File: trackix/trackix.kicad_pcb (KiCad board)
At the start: 2 copper layers, 87.6 x 114.3 mm, 42 parts, among them IC1 SIM808, J1 GSM, J2 GPS, J3 SIM5060-6-0-26-01-X_REVC, J4 AVR-ISP-6, Q1 2N3904, Q2 2N3904, U1 ATmega328P-AU

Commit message: layout changes 1
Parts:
- removed 8MHz1: Crystal, Crystal:Crystal_SMD_HC49-SD_HandSoldering
- removed D1: netstat LED, LED_SMD:LED_0805_2012Metric_Pad1.15x1.40mm_HandSolder
- removed D2: led 13, LED_SMD:LED_0805_2012Metric_Pad1.15x1.40mm_HandSolder
- removed D3: ISP led, LED_SMD:LED_0805_2012Metric_Pad1.15x1.40mm_HandSolder
- removed reset1: reset, Button_Switch_SMD:SW_SPST_TL3342
- added 13_blk: led 13, LED_SMD:LED_0805_2012Metric_Pad1.15x1.40mm_HandSolder, F.Cu at (102.2, 41.3)
- added 8MHz: Crystal, Crystals:Crystal_HC49-4H_Vertical, F.Cu at (129.2, 66.9)
- added ISP_pwr: ISP led, LED_SMD:LED_0805_2012Metric_Pad1.15x1.40mm_HandSolder, F.Cu at (102.2, 38.7)
- added RESET: reset, Buttons_Switches_SMD:SW_SPST_B3U-1000P, F.Cu at (128.3, 41.9)
- added netstat: netstat LED, LED_SMD:LED_0805_2012Metric_Pad1.15x1.40mm_HandSolder, F.Cu at (69.8, 38.7)
- J3: value SIM5060-6-0-26-01-X_REVC -> SIM CARD; footprint SIM5060-6-0-26-01-X_REVC:GCT_SIM5060-6-0-26-01-X_REVC -> SIM7100-6-1-15-00-X_REVA:GCT_SIM7100-6-1-15-00-X_REVA
- LS1: value CBT-09427-SMT -> buzzer
- moved BT1 194.6 mm to (52.7, 69.8), turned to 270 degrees
- moved C9 193.9 mm to (52.2, 54.3)
- moved C8 190.1 mm to (52.2, 56.9)
- moved C14 189.6 mm to (50.8, 67.3), turned to 180 degrees
- moved R4 186.9 mm to (65.4, 40.6), turned to 22 degrees
- moved JP1 185.6 mm to (61.0, 65.4), turned to 22 degrees
- moved R7 165.4 mm to (97.8, 41.3), turned to 180 degrees
- moved LS1 165.2 mm to (115.6, 49.5), turned to 90 degrees
- moved Q1 163.6 mm to (116.2, 40.0)
- moved R5 163.1 mm to (111.8, 40.0), turned to 90 degrees
- moved C6 160.6 mm to (52.8, 61.9)
- moved C13 160.0 mm to (51.4, 64.8), turned to 180 degrees
- moved C7 157.4 mm to (52.8, 59.4)
- moved C12 145.3 mm to (112.4, 67.5), turned to 270 degrees
- moved R8 136.1 mm to (97.8, 38.7)
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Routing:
- net Net-(J4-Pad2): track 0.00 -> 90.9 mm, vias 0 -> 2
- net Net-(D4-Pad1): track 0.00 -> 84.7 mm, vias 0 -> 1
- net Net-(C2-Pad1): track 0.00 -> 44.3 mm
- net Net-(J4-Pad3): track 0.00 -> 43.2 mm, vias 0 -> 1
- net Net-(R9-Pad1): track 0.00 -> 42.5 mm, vias 0 -> 4
- net Net-(J4-Pad5): track 0.00 -> 38.5 mm, vias 0 -> 3
- net Net-(R5-Pad1): track 0.00 -> 32.8 mm, vias 0 -> 4
- net Net-(J3-PadC7): track 0.00 -> 19.2 mm
- net Net-(J3-PadC2): track 0.00 -> 17.3 mm
- net Net-(C1-Pad1): track 0.00 -> 15.9 mm
- net Net-(C3-Pad1): track 0.00 -> 15.6 mm
- net Net-(J3-PadC3): track 0.00 -> 13.9 mm
- net +BATT: track 0.00 -> 13.3 mm
- net Net-(D1-Pad2): track 0.00 -> 12.9 mm
- net Net-(C4-Pad1): track 0.00 -> 12.9 mm
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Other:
- board size 87.6 x 114.3 mm -> 85.1 x 43.2 mm

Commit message: layout changes 2
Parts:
- removed 13_blk: led 13, LED_SMD:LED_0805_2012Metric_Pad1.15x1.40mm_HandSolder
- removed ISP_pwr: ISP led, LED_SMD:LED_0805_2012Metric_Pad1.15x1.40mm_HandSolder
- removed the netstat at (69.8, 38.7)
- added ISPpwr: ISP led, LEDs:LED_0805_HandSoldering, F.Cu at (102.2, 38.7)
- added R10: 470, Resistors_SMD:R_0805_HandSoldering, F.Cu at (52.7, 44.5)
- added R11: 470, Resistors_SMD:R_0805_HandSoldering, F.Cu at (126.4, 45.7)
- added R12: 470, Resistors_SMD:R_0805_HandSoldering, F.Cu at (97.8, 48.9)
- added blk: led 13, LEDs:LED_0805_HandSoldering, F.Cu at (102.2, 41.3)
- added netstat: netstat LED, LEDs:LED_0805_HandSoldering, F.Cu at (70.5, 38.7)
- J3: value SIM CARD -> SIM SLOT
- LS1: value buzzer -> BUZZER
- moved R4 0.63 mm to (65.4, 41.3)
- moved RESET 0.63 mm to (128.9, 41.9)
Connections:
- D4 pad 2: +BATT -> Net-(D4-Pad2)
- D5 pad 2: +BATT -> Net-(D5-Pad2)
- D6 pad 2: +BATT -> Net-(D6-Pad2)
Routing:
- net GND: track 0.00 -> 142.3 mm, vias 0 -> 43
- net +BATT: track 13.3 -> 89.8 mm, vias 0 -> 2
- net simTX: track 0.00 -> 59.2 mm, vias 0 -> 2
- net simRX: track 0.00 -> 58.7 mm, vias 0 -> 3
- net Net-(D4-Pad2): track 0.00 -> 9.41 mm
- net Net-(D6-Pad2): track 0.00 -> 5.94 mm
- net Net-(J4-Pad5): track 38.5 -> 43.6 mm, vias 3 -> 2
- net Net-(D5-Pad2): track 0.00 -> 3.21 mm
- net Net-(D1-Pad2): track 12.9 -> 12.0 mm
- net Net-(D1-Pad1): track 3.10 -> 3.67 mm
- net Net-(R9-Pad1): track 42.5 -> 42.6 mm, vias 4 -> 3
- added copper zone on B.Cu, net GND

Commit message: prototype 0.1 state
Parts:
- added G***: LOGO, Logo:LOGO, B.Cu at (74.9, 55.9)
- added U2: SIM-ST-MFF2, SIM-ST-MFF2:PSON127P500X600X82-9N, B.Cu at (102.2, 61.6)
- moved R12 2.54 mm to (97.8, 51.4), turned to 90 degrees
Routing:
- net +BATT: track 89.8 -> 156.5 mm
- net GND: track 142.3 -> 169.2 mm, vias 43 -> 44
- net Net-(J3-PadC3): track 13.9 -> 27.3 mm, vias 0 -> 1
- net Net-(J3-PadC2): track 17.3 -> 28.6 mm, vias 0 -> 1
- net Net-(C2-Pad1): track 44.3 -> 55.6 mm, vias 0 -> 1
- net Net-(J3-PadC7): track 19.2 -> 27.9 mm, vias 0 -> 1
- net (no net): track 7.47 -> 0.37 mm
- net Net-(D6-Pad2): track 5.94 -> 7.84 mm
- net Net-(J3-PadC6): track 0.00 -> 1.73 mm, vias 0 -> 1
- added copper zone on F.Cu, net +BATT
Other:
- outline, holes or cut-outs redrawn
- board text added: "trackix v.0.1 2019-02-18"

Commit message: all things so far
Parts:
- removed 8MHz: Crystal, Crystals:Crystal_HC49-4H_Vertical
- removed BT1: Li-Ion 3,7v, Connector_PinHeader_2.54mm:PinHeader_1x02_P2.54mm_Horizontal
- removed IC1: SIM808, QFN100P2400X2400X260-68N
- removed ISPpwr: ISP led, LEDs:LED_0805_HandSoldering
- removed LS1: BUZZER, CUI_CBT-09427-SMT
- removed Q2: 2N3904, Package_TO_SOT_SMD:SOT-23_Handsoldering
- removed R3: 22, Resistor_SMD:R_0805_2012Metric_Pad1.15x1.40mm_HandSolder
- removed R4: 470, Resistor_SMD:R_0805_2012Metric_Pad1.15x1.40mm_HandSolder
- removed RESET: reset, Buttons_Switches_SMD:SW_SPST_B3U-1000P
- removed blk: led 13, LEDs:LED_0805_HandSoldering
- removed netstat: netstat LED, LEDs:LED_0805_HandSoldering
- added 8MHz1: Crystal, Crystals:Crystal_HC49-U_Vertical, F.Cu at (106.2, 63.0)
- added BZ1: Buzzer, Buzzers_Beepers:Buzzer_Murata_PKMCS0909E4000-R1, F.Cu at (140.0, 65.8)
- added C15: 10uF, Capacitors_SMD:C_1206, F.Cu at (77.5, 60.5)
- added C16: 100nF, Capacitors_SMD:C_0603, F.Cu at (95.0, 65.5)
- added C17: C_100nF, Capacitors_SMD:C_0603, F.Cu at (114.5, 41.5)
- added D1: GPS_LED, LEDs:LED_0805, F.Cu at (116.8, 44.8)
- added D10: D_B5818WS SK, Diodes_SMD:D_SOD-323, F.Cu at (64.2, 65.8)
- added D11: D_B5818WS SK, Diodes_SMD:D_SOD-323, F.Cu at (67.8, 65.3)
- added D2: led 13, LEDs:LED_0805, F.Cu at (115.8, 68.5)
- added D3: D_B5818WS SK, Diodes_SMD:D_SOD-323, F.Cu at (64.5, 68.2)
- added D7: LED_chrg, LEDs:LED_0805, F.Cu at (64.2, 63.7)
- added D8: LED_stdby, LEDs:LED_0805, F.Cu at (64.2, 61.7)
- added D9: D_B5818WS SK, Diodes_SMD:D_SOD-323, F.Cu at (68.2, 68.2)
- added H1: DYNAMO_A, Mounting_Holes:MountingHole_2.2mm_M2_ISO14580_Pad, F.Cu at (71.5, 76.5)
- added H2: DYNAMO_B, Mounting_Holes:MountingHole_2.2mm_M2_ISO14580_Pad, F.Cu at (77.2, 76.5)
- added IC2: TP4056, Housings_SOIC:HTSOP-8-1EP_3.9x4.9mm_Pitch1.27mm_ThermalVias_LargeCopper, F.Cu at (78.0, 64.8)
- added JP3: MOSI, Jumper:SolderJumper-2_P1.3mm_Open_RoundedPad1.0x1.5mm, F.Cu at (95.0, 47.5)
- added JP4: MISO, Jumper:SolderJumper-2_P1.3mm_Open_RoundedPad1.0x1.5mm, F.Cu at (95.0, 49.8)
- added L1: L27nH, Inductors_SMD:L_0402, F.Cu at (138.5, 52.0)
- added L2: L2.2uH, Inductors_SMD:L_1210, F.Cu at (89.2, 68.2)
- added Q3: FS8205A, Housings_SSOP:TSSOP-8_4.4x3mm_Pitch0.65mm, F.Cu at (81.0, 55.8)
- added Q5: 2N3904, TO_SOT_Packages_SMD:SOT-23, F.Cu at (102.3, 50.0)
- added R13: 470, Resistors_SMD:R_0603, F.Cu at (68.5, 61.5)
- added R14: 470, Resistors_SMD:R_0603, F.Cu at (68.2, 59.8)
- added R15: 4k for Ibat 300mA, Resistors_SMD:R_0603, F.Cu at (83.2, 66.2)
- added R16: R100, Resistors_SMD:R_0603, F.Cu at (122.5, 60.0)
- added R17: R22, Resistors_SMD:R_0603, F.Cu at (137.5, 50.0)
- added R18: R100, Resistors_SMD:R_0603, F.Cu at (120.2, 45.8)
- added R19: R5k, Resistors_SMD:R_0603, F.Cu at (100.0, 61.2)
- added R20: R10k, Resistors_SMD:R_0603, F.Cu at (100.8, 64.2)
- added R21: 4.7k, Resistors_SMD:R_0603, F.Cu at (110.9, 36.9)
- added TP1: DYNAMO_A, Connectors_TestPoints:Test_Point_Pad_1.0x1.0mm, B.Cu at (71.5, 72.2)
- added TP2: DYNAMO_B, Connectors_TestPoints:Test_Point_Pad_1.0x1.0mm, B.Cu at (77.2, 72.2)
- added TP3: GND, Connectors_TestPoints:Test_Point_Pad_1.0x1.0mm, B.Cu at (87.3, 68.4)
- added TP4: VCC_IN_DC, Connectors_TestPoints:Test_Point_Pad_1.0x1.0mm, B.Cu at (102.0, 67.5)
- added TP5: AUX_ON, Connectors_TestPoints:Test_Point_Pad_1.0x1.0mm, B.Cu at (92.0, 60.0)
- added TP6: GPS_TX, Connectors_TestPoints:Test_Point_Pad_1.0x1.0mm, B.Cu at (125.0, 60.5)
- added TP7: TX, Connectors_TestPoints:Test_Point_Pad_1.0x1.0mm, B.Cu at (109.5, 52.0)
- added TP8: RX, Connectors_TestPoints:Test_Point_Pad_1.0x1.0mm, B.Cu at (104.5, 52.0)
- added TP9: TestPoint3.3V, Connectors_TestPoints:Test_Point_Pad_1.0x1.0mm, B.Cu at (92.3, 68.4)
- added U3: DW-01, TO_SOT_Packages_SMD:TSOT-23-6, F.Cu at (73.8, 57.2)
- added U4: TPS62291DRVR, user_added_kicad_libs:SON65P200X200X80-7N, F.Cu at (89.5, 64.8)
- added U5: RFM95W-868S2, RF_Modules:Hopref_RFM9XW_SMD, F.Cu at (82.5, 44.0)
- added U6: ADXL345BCCZ, Housings_LGA:Bosch_LGA-14_3x2.5mm_Pitch0.5mm, F.Cu at (114.5, 38.0)
- added reset1: reset, Buttons_Switches_SMD:SW_SPST_B3U-1000P, F.Cu at (144.5, 38.5)
- C1: value 22pF -> 100nF; footprint Capacitor_SMD:C_0805_2012Metric_Pad1.15x1.40mm_HandSolder -> Capacitors_SMD:C_0805
- C10, C11: footprint Capacitor_SMD:C_0805_2012Metric_Pad1.15x1.40mm_HandSolder -> Capacitors_SMD:C_0402
- C12: value 0,1uF -> 10uF; footprint Capacitor_SMD:C_0805_2012Metric_Pad1.15x1.40mm_HandSolder -> Capacitors_SMD:C_1206
- C13: footprint Capacitor_Tantalum_SMD:CP_EIA-3216-10_Kemet-I_Pad1.58x1.35mm_HandSolder -> Capacitors_SMD:C_0603
- C14: value 0,1uF -> 0.1uF; footprint Capacitor_SMD:C_0805_2012Metric_Pad1.15x1.40mm_HandSolder -> Capacitors_SMD:C_0603
- C2: value 1uF -> 10uF; footprint Capacitor_Tantalum_SMD:CP_EIA-3216-10_Kemet-I_Pad1.58x1.35mm_HandSolder -> Capacitors_SMD:C_1206
- C3: value 22pF -> C_100nF; footprint Capacitor_SMD:C_0805_2012Metric_Pad1.15x1.40mm_HandSolder -> Capacitors_SMD:C_0603
- C4: value 22pF -> C_4.7uF; footprint Capacitor_SMD:C_0805_2012Metric_Pad1.15x1.40mm_HandSolder -> Capacitors_SMD:C_1206
- C5: value 1uF -> C_100nF; footprint Capacitor_Tantalum_SMD:CP_EIA-3216-10_Kemet-I_Pad1.58x1.35mm_HandSolder -> Capacitors_SMD:C_0603
- C6: value 100uF -> C_4.7uF; footprint Capacitor_Tantalum_SMD:CP_EIA-3216-10_Kemet-I_Pad1.58x1.35mm_HandSolder -> Capacitors_SMD:C_1206
- C7: value 10uF -> C_100nF; footprint Capacitor_Tantalum_SMD:CP_EIA-3216-10_Kemet-I_Pad1.58x1.35mm_HandSolder -> Capacitors_SMD:C_0603
- C8: value 33pF -> 100nF; footprint Capacitor_SMD:C_0805_2012Metric_Pad1.15x1.40mm_HandSolder -> Capacitors_SMD:C_0603
- C9: value 10pF -> 10uF; footprint Capacitor_SMD:C_0805_2012Metric_Pad1.15x1.40mm_HandSolder -> Capacitors_SMD:C_1206
- D4, D5: footprint LED_THT:LED_D5.0mm_Horizontal_O6.35mm_Z15.0mm -> LEDs:LED_D5.0mm_Horizontal_O1.27mm_Z3.0mm
- D6: footprint LED_THT:LED_D5.0mm_FlatTop -> LEDs:LED_D5.0mm
- J1: value GSM -> BATTERY; footprint Connector_Coaxial:U.FL_Hirose_U.FL-R-SMT-1_Vertical -> Pin_Headers:Pin_Header_Straight_1x02_Pitch2.54mm
- J2: footprint Connector_Coaxial:U.FL_Hirose_U.FL-R-SMT-1_Vertical -> Connectors_Molex:Molex_Microcoaxial_RF
- J3: value SIM SLOT -> LORA_868; footprint SIM7100-6-1-15-00-X_REVA:GCT_SIM7100-6-1-15-00-X_REVA -> Connectors_Molex:Molex_Microcoaxial_RF
- J4: footprint Connector_PinSocket_2.54mm:PinSocket_2x03_P2.54mm_Vertical -> Socket_Strips:Socket_Strip_Straight_2x03_Pitch2.54mm_SMD
- JP1: value Power Selector -> SCK; footprint Connector_PinSocket_2.54mm:PinSocket_1x03_P2.54mm_Vertical -> Jumper:SolderJumper-2_P1.3mm_Open_RoundedPad1.0x1.5mm
- Q1: footprint Package_TO_SOT_SMD:SOT-23_Handsoldering -> TO_SOT_Packages_SMD:SOT-23
- R1: value 22 -> 100; footprint Resistor_SMD:R_0805_2012Metric_Pad1.15x1.40mm_HandSolder -> Resistors_SMD:R_0603
- R10, R11, R12: value 470 -> 330; footprint Resistors_SMD:R_0805_HandSoldering -> Resistors_SMD:R_0603
- R2: value 22 -> 1k; footprint Resistor_SMD:R_0805_2012Metric_Pad1.15x1.40mm_HandSolder -> Resistors_SMD:R_0603
- R5, R6, R9: footprint Resistor_SMD:R_0805_2012Metric_Pad1.15x1.40mm_HandSolder -> Resistors_SMD:R_0603
- R7: value 470 -> 330; footprint Resistor_SMD:R_0805_2012Metric_Pad1.15x1.40mm_HandSolder -> Resistors_SMD:R_0603
- R8: value 470 -> 4.7k; footprint Resistor_SMD:R_0805_2012Metric_Pad1.15x1.40mm_HandSolder -> Resistors_SMD:R_0603
- U1: footprint Package_QFP:TQFP-32_7x7mm_P0.8mm -> Housings_QFP:TQFP-32_7x7mm_Pitch0.8mm
- U2: value SIM-ST-MFF2 -> SIM28ML; footprint SIM-ST-MFF2:PSON127P500X600X82-9N -> SIM28ML:XCVR_SIM28ML; moved to F.Cu
- moved C6 74.7 mm to (125.0, 42.8)
- moved C7 72.5 mm to (122.5, 39.5), turned to 90 degrees
- moved C8 65.7 mm to (117.8, 53.2), turned to 315 degrees
- moved J2 47.9 mm to (138.5, 56.0), turned to 180 degrees
- moved J3 42.9 mm to (67.2, 39.0), turned to 90 degrees
- moved C4 41.9 mm to (120.8, 49.5), turned to 90 degrees
- moved JP1 39.6 mm to (95.0, 45.2), turned to 0 degrees
- moved C9 37.3 mm to (88.8, 61.5), turned to 180 degrees
- moved C5 36.1 mm to (118.5, 49.0), turned to 90 degrees
- moved R7 32.4 mm to (118.5, 66.2), turned to 0 degrees
- moved R5 31.0 mm to (132.2, 63.2), turned to 180 degrees
- moved Q1 30.4 mm to (132.0, 66.0), turned to 270 degrees
- moved U2 29.4 mm to (129.2, 50.0)
- moved C11 26.2 mm to (104.1, 66.1), turned to 135 degrees
- moved C10 26.0 mm to (106.1, 68.1), turned to 315 degrees
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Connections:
- net Net-(J4-Pad5) renamed RESET
- C1 pad 1: Net-(C1-Pad1) -> CHARGE_DETECT
- C12 pad 1: Net-(C12-Pad1) -> +3V3
- C2 pad 1: Net-(C2-Pad1) -> +BATT
- C3 pad 2: GND -> -BATT
- C4 pad 1: Net-(C4-Pad1) -> +3V3
- C5 pad 1: Net-(C2-Pad1) -> +3V3
- C6 pad 1: GND -> Net-(C6-Pad1)
- C6 pad 2: +BATT -> GND
- C7 pad 1: GND -> Net-(C6-Pad1)
- C7 pad 2: +BATT -> GND
- C8 pad 2: +BATT -> Net-(C8-Pad2)
- C9 pad 1: GND -> +BATT
- C9 pad 2: +BATT -> GND
- J1 pad 1: Net-(IC1-Pad66) -> -BATT
- J1 pad 2: GND -> +BATT
- J2 pad 1: Net-(IC1-Pad35) -> Net-(J2-Pad1)
- J3 pad 1: (no net) -> Net-(J3-Pad1)
- J3 pad 2: (no net) -> GND
- JP1 pad 1: Net-(J4-Pad2) -> SCK
- JP1 pad 2: +BATT -> Net-(J4-Pad3)
- R1 pad 1: Net-(J3-PadC7) -> Net-(C3-Pad1)
- R1 pad 2: Net-(C1-Pad1) -> +BATT
- R2 pad 1: Net-(J3-PadC3) -> Net-(R2-Pad1)
- R2 pad 2: Net-(C3-Pad1) -> GND
- R5 pad 1: Net-(R5-Pad1) -> DRIVE_BUZZER
- R8 pad 1: Net-(J4-Pad2) -> +3V3
- R8 pad 2: Net-(D3-Pad2) -> SCL
- R9 pad 1: Net-(R9-Pad1) -> DRIVE_LED
- U1 pad 1: Net-(U1-Pad1) -> DIO_1
- U1 pad 10: Net-(R9-Pad1) -> NSS
- U1 pad 11: Net-(R5-Pad1) -> AUX_ON
- U1 pad 12: simRX -> GPS_TX
- U1 pad 13: simTX -> DRIVE_LED
- U1 pad 14: Net-(U1-Pad14) -> DRIVE_BUZZER
- U1 pad 2: Net-(U1-Pad2) -> DIO_2
- U1 pad 20: Net-(C12-Pad1) -> Net-(C8-Pad2)
- U1 pad 27: Net-(U1-Pad27) -> SDA
- U1 pad 28: Net-(U1-Pad28) -> SCL
- U1 pad 32: Net-(U1-Pad32) -> DIO_0
- U1 pad 9: Net-(U1-Pad9) -> RFM_RESET
- U2 pad 2: (no net) -> Net-(R16-Pad1)
- U2 pad 3: Net-(J3-PadC7) -> GND
- U2 pad 4: (no net) -> Net-(R18-Pad2)
- U2 pad 5: (no net) -> Net-(U2-Pad5)
- U2 pad 6: Net-(J3-PadC3) -> Net-(C6-Pad1)
- U2 pad 7: Net-(J3-PadC2) -> Net-(U2-Pad7)
- U2 pad 8: Net-(C2-Pad1) -> +3V3
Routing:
- net +3V3: track 0.00 -> 176.5 mm, vias 0 -> 1
- net Net-(J4-Pad2): track 90.9 -> 0.00 mm, vias 2 -> 0
- net GND: track 169.2 -> 82.2 mm, vias 44 -> 174
- net CHARGE_DETECT: track 0.00 -> 84.1 mm, vias 0 -> 1
- net simTX: track 59.2 -> 0.00 mm, vias 2 -> 0
- net simRX: track 58.7 -> 0.00 mm, vias 3 -> 0
- net DRIVE_LED: track 0.00 -> 58.5 mm
- net Net-(C2-Pad1): track 55.6 -> 0.00 mm, vias 1 -> 0
- net RFM_RESET: track 0.00 -> 52.3 mm, vias 0 -> 2
- net Net-(J4-Pad4): track 6.37 -> 52.9 mm, vias 0 -> 2
- net DIO_0: track 0.00 -> 44.2 mm, vias 0 -> 2
- net Net-(R9-Pad1): track 42.6 -> 0.00 mm, vias 3 -> 0
- net AUX_ON: track 0.00 -> 41.7 mm, vias 0 -> 2
- net NSS: track 0.00 -> 40.7 mm, vias 0 -> 2
- net DIO_1: track 0.00 -> 38.8 mm, vias 0 -> 2
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- added copper zone on F.Cu, net +3V3
- added copper zone on B.Cu, net DYNAMO_A
- added copper zone on F.Cu, net DYNAMO_A
- added copper zone on B.Cu, net DYNAMO_B
- added copper zone on F.Cu, net DYNAMO_B
- added copper zone on F.Cu, net GND
- added copper zone on F.Cu, net Net-(L2-Pad1)
- removed copper zone on F.Cu, net +BATT
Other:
- board size 85.1 x 43.2 mm -> 85.1 x 43.3 mm
- rule trace_min: 0.2 -> 0.1
- board text added: "3.3V"
- board text added: "AUX EN"
- board text added: "GND"
- board text added: "GPS ANTENNA LOCATION"
- board text added: "GPS TX"
- board text added: "RX"
- board text added: "TX"
- board text added: "VCC DC"
- board text added: "trackix V_0.2 2020-05-04"
- board text removed: "trackix v.0.1 2019-02-18"

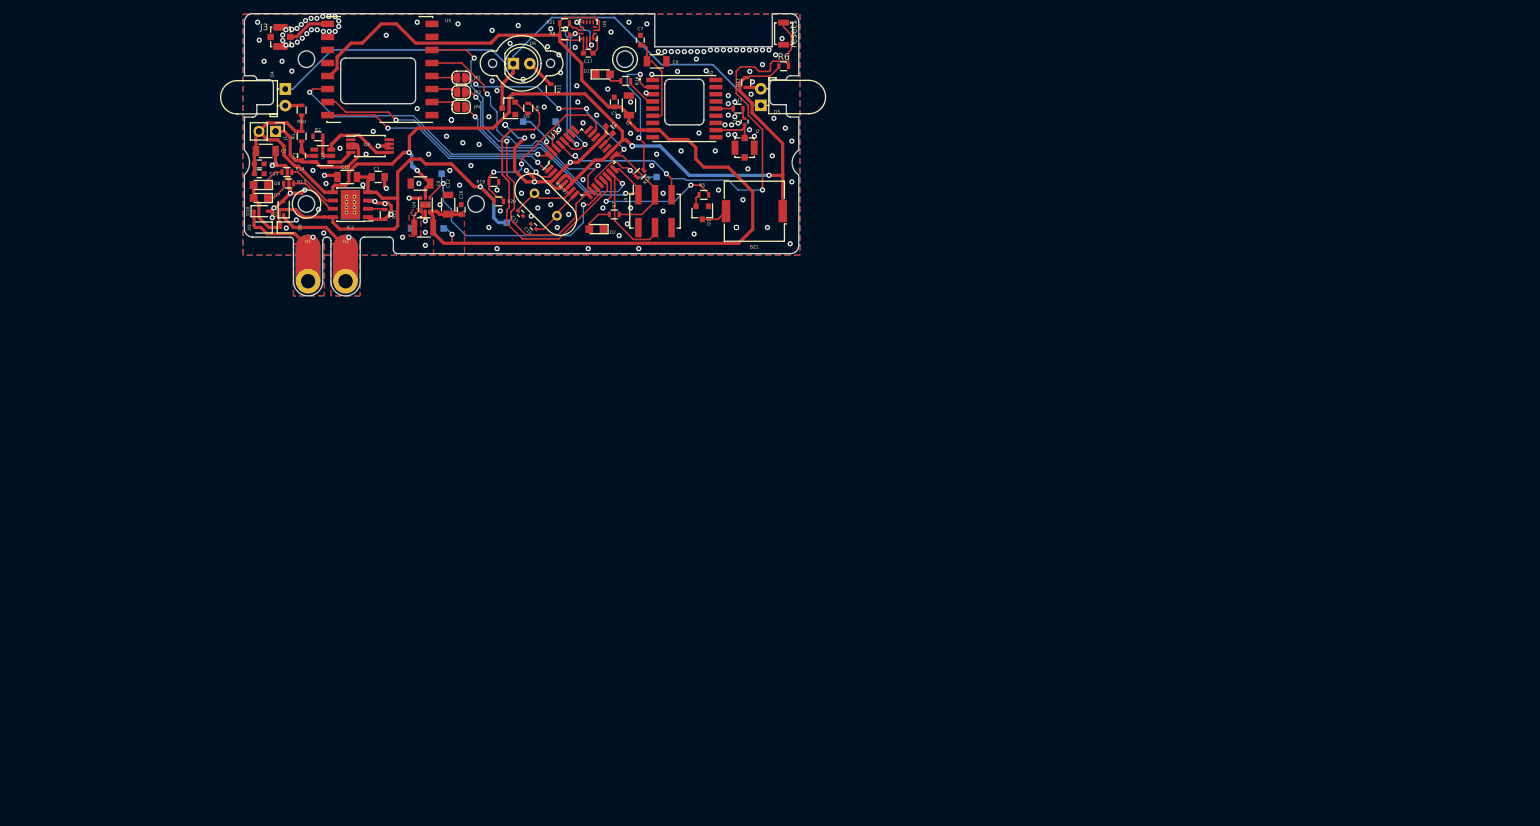
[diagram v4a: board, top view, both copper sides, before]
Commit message: added gsm version
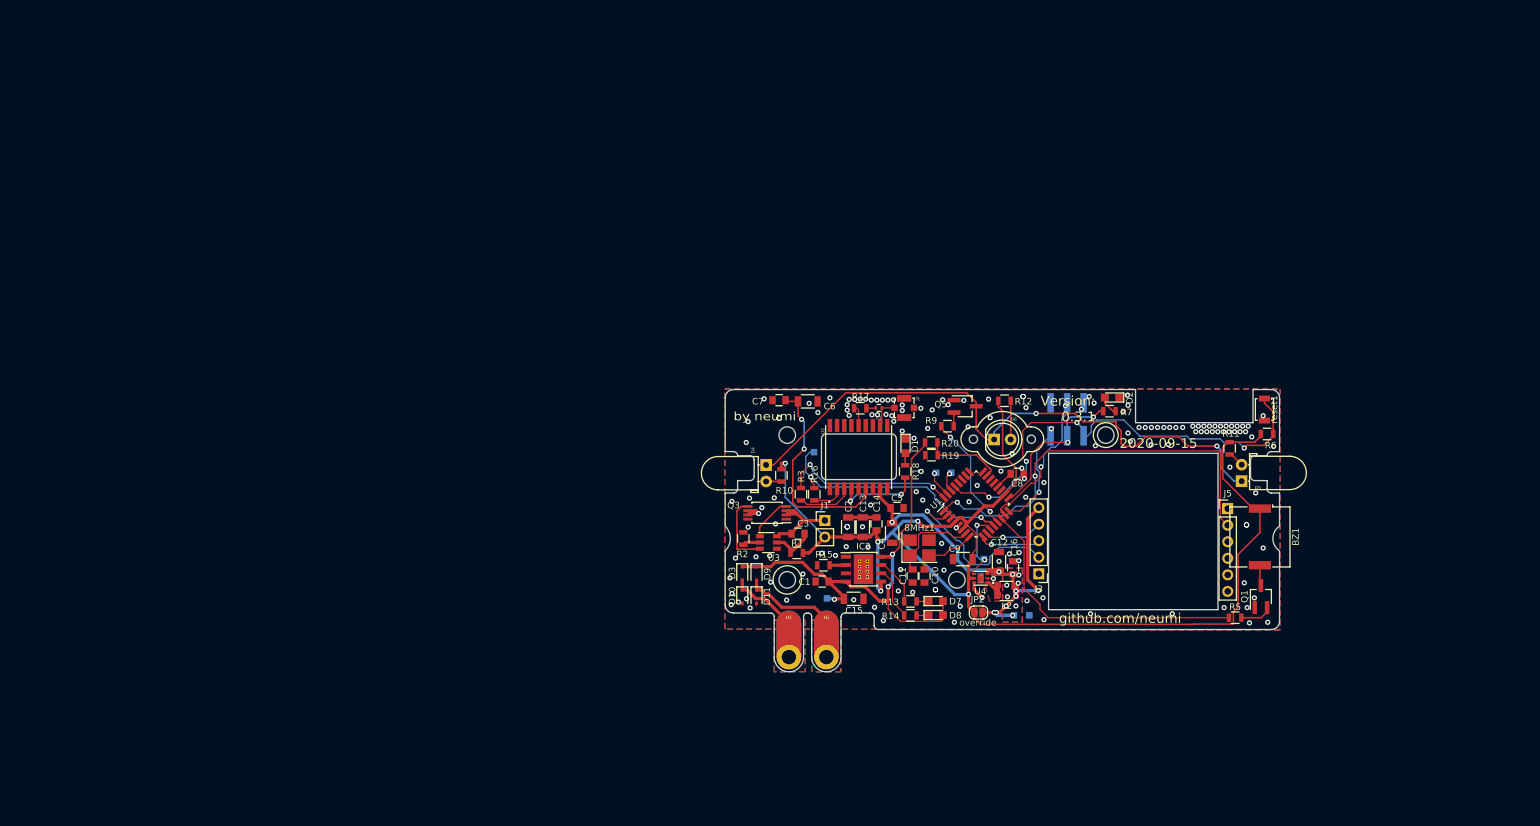
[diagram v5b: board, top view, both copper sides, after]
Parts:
- removed C17: C_100nF, Capacitors_SMD:C_0603
- removed G***: LOGO, Logo:LOGO
- removed JP1: SCK, Jumper:SolderJumper-2_P1.3mm_Open_RoundedPad1.0x1.5mm
- removed JP3: MOSI, Jumper:SolderJumper-2_P1.3mm_Open_RoundedPad1.0x1.5mm
- removed JP4: MISO, Jumper:SolderJumper-2_P1.3mm_Open_RoundedPad1.0x1.5mm
- removed R21, R8: 4.7k, Resistors_SMD:R_0603
- removed U5: RFM95W-868S2, RF_Modules:Hopref_RFM9XW_SMD
- removed U6: ADXL345BCCZ, Housings_LGA:Bosch_LGA-14_3x2.5mm_Pitch0.5mm
- added J5: Conn_01x06_Male, Pin_Headers:Pin_Header_Straight_1x06_Pitch2.54mm, F.Cu at (212.7, 111.4)
- added JP2: PWR_BRIDGE, Jumper:SolderJumper-2_P1.3mm_Open_RoundedPad1.0x1.5mm, F.Cu at (174.4, 127.3)
- added R3: R100, Resistors_SMD:R_0805, F.Cu at (147.2, 109.2)
- 8MHz1: footprint Crystals:Crystal_HC49-U_Vertical -> Crystals:Crystal_SMD_3225-4pin_3.2x2.5mm_HandSoldering
- C10, C11: footprint Capacitors_SMD:C_0402 -> Capacitors_SMD:C_0805
- C13: footprint Capacitors_SMD:C_0603 -> Capacitors_SMD:C_1206
- C14, C16, C3, C5, C7, C8: footprint Capacitors_SMD:C_0603 -> Capacitors_SMD:C_0805
- J3: value LORA_868 -> Conn_01x05_Male; footprint Connectors_Molex:Molex_Microcoaxial_RF -> Pin_Headers:Pin_Header_Straight_1x05_Pitch2.54mm
- J4: moved to B.Cu
- Q1, Q5: footprint TO_SOT_Packages_SMD:SOT-23 -> TO_SOT_Packages_SMD:SOT-23W_Handsoldering
- R1, R10, R11, R12, R13, R14, R15, R16, R17, R18, R19, R2, R20, R5, R6, R7, R9: footprint Resistors_SMD:R_0603 -> Resistors_SMD:R_0805
- moved J3 142.6 mm to (183.7, 121.4), turned to 180 degrees
- moved D8 122.9 mm to (167.8, 127.8), turned to 0 degrees
- moved D7 120.7 mm to (167.8, 125.6), turned to 0 degrees
- moved R14 117.4 mm to (163.9, 127.8), turned to 0 degrees
- moved R13 115.0 mm to (163.9, 125.7), turned to 0 degrees
- moved TP3 112.0 mm to (182.2, 127.8), turned to 0 degrees
- moved C14 108.9 mm to (158.8, 113.8), turned to 90 degrees
- moved C13 108.1 mm to (156.7, 114.2), turned to 90 degrees
- moved C2 106.4 mm to (154.4, 114.2), turned to 90 degrees
- moved TP9 105.8 mm to (179.8, 127.8)
- moved L2 105.4 mm to (178.7, 124.0)
- moved R5 104.2 mm to (213.8, 128.2), turned to 0 degrees
- moved Q1 104.0 mm to (217.8, 124.9), turned to 90 degrees
- moved J1 103.3 mm to (150.8, 113.2), turned to 0 degrees
- moved U4 102.7 mm to (174.8, 122.1), turned to 180 degrees
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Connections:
- J3 pad 1: Net-(J3-Pad1) -> GND
- J3 pad 2: GND -> sim_rx
- U1 pad 1: DIO_1 -> sim_dtr
- U1 pad 10: NSS -> sim_rst
- U1 pad 2: DIO_2 -> sim_rx
- U1 pad 32: DIO_0 -> GPS_RX
- U1 pad 9: RFM_RESET -> sim_tx
- U2 pad 3: GND -> Net-(R3-Pad1)
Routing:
- net +3V3: track 176.5 -> 69.1 mm, vias 1 -> 15
- net GND: track 82.2 -> 11.6 mm, vias 174 -> 164
- net sim_dtr: track 0.00 -> 62.9 mm, vias 0 -> 2
- net RFM_RESET: track 52.3 -> 0.00 mm, vias 2 -> 0
- net DIO_0: track 44.2 -> 0.00 mm, vias 2 -> 0
- net NSS: track 40.7 -> 0.00 mm, vias 2 -> 0
- net DRIVE_LED: track 58.5 -> 18.4 mm, vias 0 -> 2
- net DIO_1: track 38.8 -> 0.00 mm, vias 2 -> 0
- net DIO_2: track 38.8 -> 0.00 mm, vias 2 -> 0
- net Net-(J4-Pad4): track 52.9 -> 22.7 mm
- net AUX_ON: track 41.7 -> 11.8 mm
- net sim_rx: track 0.00 -> 27.7 mm, vias 0 -> 1
- net GPS_RX: track 0.00 -> 27.2 mm, vias 0 -> 2
- net +BATT: track 173.4 -> 198.7 mm
- net SCL: track 24.8 -> 0.00 mm, vias 2 -> 0
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- added copper zone on B.Cu, net +3V3
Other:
- outline, holes or cut-outs redrawn
- board text added: "2020-09-15"
- board text added: "AUX_ON"
- board text added: "GPS_TX"
- board text added: "ISP"
- board text added: "SIM800L"
- board text added: "VCC_IN_DC"
- board text added: "Version: 0.3.1"
- board text added: "by neumi"
- board text added: "github.com/neumi"
- board text added: "override"
- board text removed: "AUX EN"
- board text removed: "GPS TX"
- board text removed: "VCC DC"
- board text removed: "trackix V_0.2 2020-05-04"
